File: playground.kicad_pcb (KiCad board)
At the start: 2 copper layers, 80 x 50 mm, 56 parts, among them IC1 TXU0101DBVR, IC11 LM3940IMP-3.3_NOPB, IC2 TXU0101DBVR, IC3 TXU0101DBVR, IC4 TXU0101DBVR, IC5 TXU0101DBVR, IC6 TXU0101DBVR, IC7 TXU0101DBVR, IC8 TXU0101DBVR, IC9 L293DD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

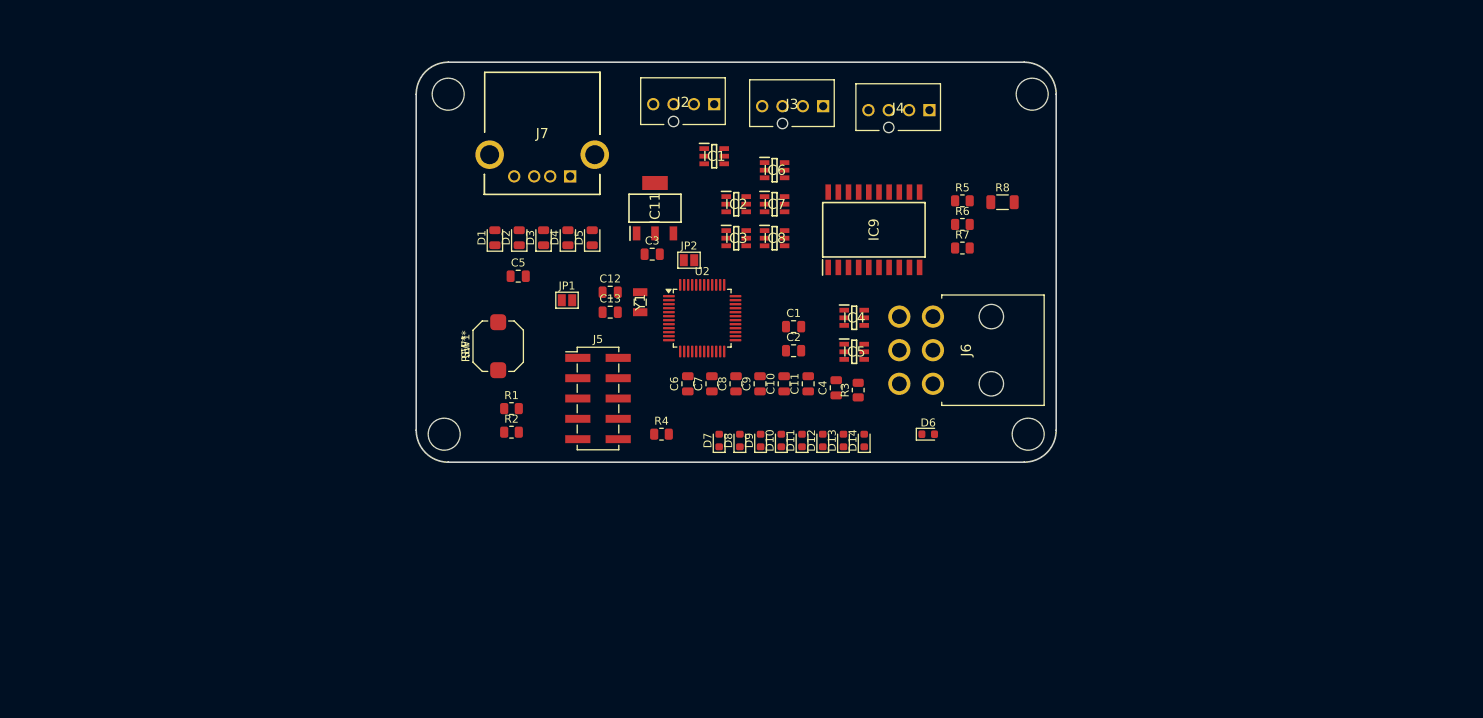
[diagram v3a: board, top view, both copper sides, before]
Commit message: Added LEDs and testpoints
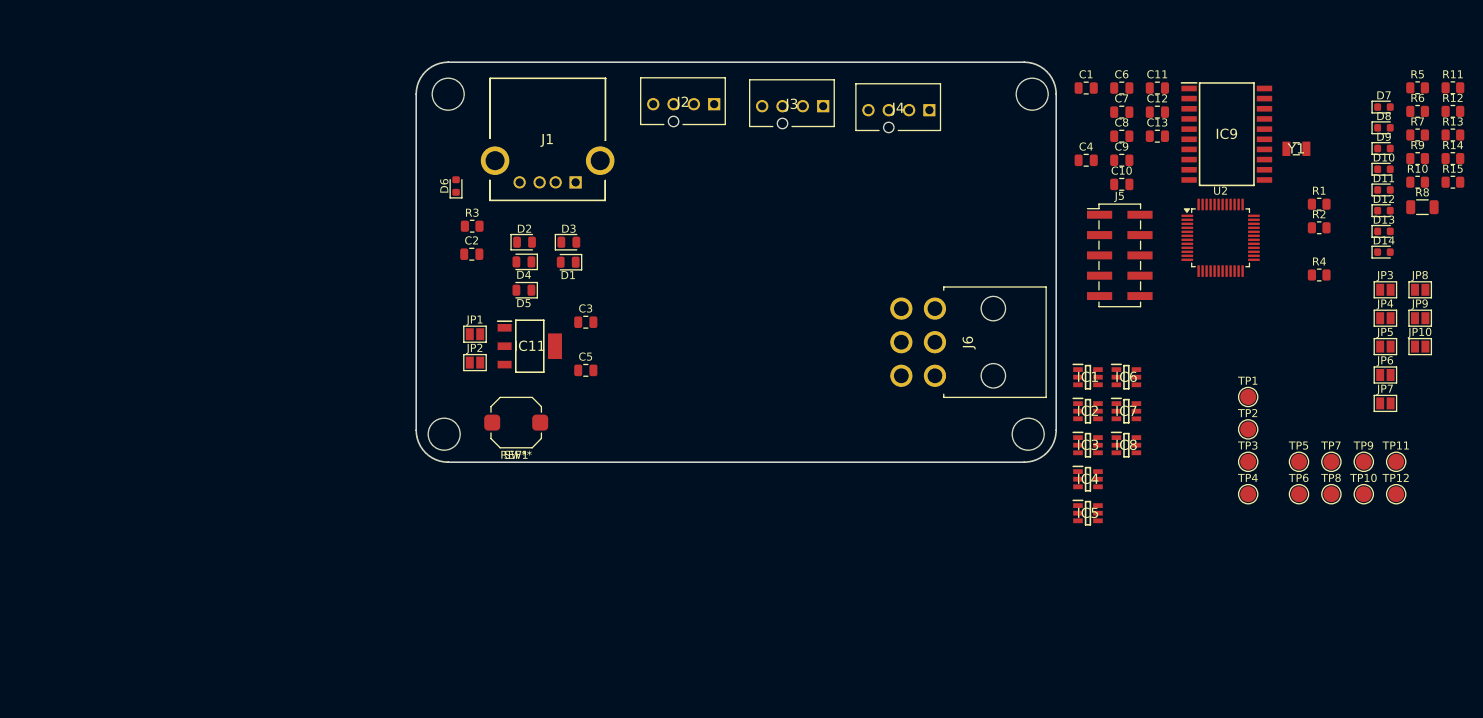
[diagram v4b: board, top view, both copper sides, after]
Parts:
- removed J7: USB_A, custom_footprints:676432910
- added J1: 67643-2910, custom_footprints:676432910, F.Cu at (119.9, 65.0)
- added JP10: SolderJumper_2_Open, Jumper:SolderJumper-2_P1.3mm_Open_Pad1.0x1.5mm, F.Cu at (225.5, 85.5)
- added JP3: SolderJumper_2_Open, Jumper:SolderJumper-2_P1.3mm_Open_Pad1.0x1.5mm, F.Cu at (221.2, 78.5)
- added JP4: SolderJumper_2_Open, Jumper:SolderJumper-2_P1.3mm_Open_Pad1.0x1.5mm, F.Cu at (221.2, 82.0)
- added JP5: SolderJumper_2_Open, Jumper:SolderJumper-2_P1.3mm_Open_Pad1.0x1.5mm, F.Cu at (221.2, 85.5)
- added JP6: SolderJumper_2_Open, Jumper:SolderJumper-2_P1.3mm_Open_Pad1.0x1.5mm, F.Cu at (221.2, 89.1)
- added JP7: SolderJumper_2_Open, Jumper:SolderJumper-2_P1.3mm_Open_Pad1.0x1.5mm, F.Cu at (221.2, 92.7)
- added JP8: SolderJumper_2_Open, Jumper:SolderJumper-2_P1.3mm_Open_Pad1.0x1.5mm, F.Cu at (225.5, 78.5)
- added JP9: SolderJumper_2_Open, Jumper:SolderJumper-2_P1.3mm_Open_Pad1.0x1.5mm, F.Cu at (225.5, 82.0)
- added R10: 51R, Resistor_SMD:R_0805_2012Metric, F.Cu at (225.2, 65.0)
- added R11: 20R, Resistor_SMD:R_0805_2012Metric, F.Cu at (229.6, 53.2)
- added R12: 20R, Resistor_SMD:R_0805_2012Metric, F.Cu at (229.6, 56.1)
- added R13: 20R, Resistor_SMD:R_0805_2012Metric, F.Cu at (229.6, 59.1)
- added R14: 20R, Resistor_SMD:R_0805_2012Metric, F.Cu at (229.6, 62.0)
- added R15: 20R, Resistor_SMD:R_0805_2012Metric, F.Cu at (229.6, 65.0)
- added R9: 51R, Resistor_SMD:R_0805_2012Metric, F.Cu at (225.2, 62.0)
- added TP1: TestPoint, TestPoint:TestPoint_Pad_D2.0mm, F.Cu at (204.0, 91.8)
- added TP10: TestPoint, TestPoint:TestPoint_Pad_D2.0mm, F.Cu at (218.4, 104.0)
- added TP11: TestPoint, TestPoint:TestPoint_Pad_D2.0mm, F.Cu at (222.5, 100.0)
- added TP12: TestPoint, TestPoint:TestPoint_Pad_D2.0mm, F.Cu at (222.5, 104.0)
- added TP2: TestPoint, TestPoint:TestPoint_Pad_D2.0mm, F.Cu at (204.0, 95.9)
- added TP3: TestPoint, TestPoint:TestPoint_Pad_D2.0mm, F.Cu at (204.0, 100.0)
- added TP4: TestPoint, TestPoint:TestPoint_Pad_D2.0mm, F.Cu at (204.0, 104.0)
- added TP5: TestPoint, TestPoint:TestPoint_Pad_D2.0mm, F.Cu at (210.3, 100.0)
- added TP6: TestPoint, TestPoint:TestPoint_Pad_D2.0mm, F.Cu at (210.3, 104.0)
- added TP7: TestPoint, TestPoint:TestPoint_Pad_D2.0mm, F.Cu at (214.4, 100.0)
- added TP8: TestPoint, TestPoint:TestPoint_Pad_D2.0mm, F.Cu at (214.4, 104.0)
- added TP9: TestPoint, TestPoint:TestPoint_Pad_D2.0mm, F.Cu at (218.4, 100.0)
- D14: value GENERAL_BOARD_1_IND -> GENERAL_BOARD_2_IND
- moved R1 104.1 mm to (212.9, 67.8)
- moved R2 104.1 mm to (212.9, 70.7)
- moved D7 93.0 mm to (221.0, 55.6), turned to 0 degrees
- moved D8 89.5 mm to (221.0, 58.2), turned to 0 degrees
- moved D9 86.0 mm to (221.0, 60.8), turned to 0 degrees
- moved R4 84.6 mm to (212.9, 76.6)
- moved Y1 84.2 mm to (210.0, 60.8), turned to 0 degrees
- moved D10 82.6 mm to (221.0, 63.4), turned to 0 degrees
- moved D11 79.2 mm to (221.0, 66.0), turned to 0 degrees
- moved D12 75.8 mm to (221.0, 68.6), turned to 0 degrees
- moved D13 72.4 mm to (221.0, 71.2), turned to 0 degrees
- moved C12 72.0 mm to (192.6, 56.2)
- moved C13 71.8 mm to (192.6, 59.2)
- moved D14 69.1 mm to (221.0, 73.7), turned to 0 degrees
- moved J5 67.6 mm to (187.9, 74.2)
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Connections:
- D1 pad 2: /USB_D+ -> /USB_D-
- D10 pad 2: /FAN_PWM_IND_LED -> /LEDs/FAN_PWM_IND_LED_5v
- D11 pad 2: /VALVE_OPEN_IND_LED -> /LEDs/VALVE_OPEN_IND_LED_5v
- D12 pad 2: /VALVE_CLOSED_IND_LED -> /LEDs/VALVE_CLOSED_IND_LED_5v
- D13 pad 2: /GENERAL_BOARD_1_IND_LED -> /LEDs/GENERAL_BOARD_1_IND_LED_3v3
- D14 pad 2: /GENERAL_BOARD_1_IND_LED -> /LEDs/GENERAL_BOARD_2_IND_LED_3v3
- D2 pad 2: /USB_D- -> /USB_D+
- D3 pad 1: /USB_D+ -> /USB_D-
- D4 pad 1: /USB_D- -> /USB_D+
- D6 pad 2: /5v_USB_PWR_IND_LED -> /LEDs/5v_USB_PWR_IND_LED
- D7 pad 2: +3V3 -> /LEDs/3v3_PWR_IND_LED
- D8 pad 2: +12V -> /LEDs/12v_PWR_IND_LED
- D9 pad 2: /PUMP_PWM_IND_LED -> /LEDs/PUMP_PWM_IND_LED_5v
- J2 pad 3: /PumpSense_5v -> Net-(JP4-B)
- J2 pad 4: /PumpCtrl_5v -> Net-(JP3-B)
- J3 pad 3: /FanSense_5v -> Net-(JP6-B)
- J3 pad 4: /FanCtrl_5v -> Net-(JP5-B)
- J4 pad 1: /ValveSense2_5v -> Net-(JP10-B)
- J4 pad 2: /ValveSense1_5v -> Net-(JP9-B)
- J4 pad 3: /ValveOutput1_12v -> Net-(JP8-B)
- J4 pad 4: /ValveOutput2_12v -> Net-(JP7-B)
- R5 pad 1: GND -> /LEDs/3v3_PWR_IND_LED
- R8 pad 2: unconnected-(R8-Pad2) -> /LEDs/12v_PWR_IND_LED

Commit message: removed jumpers
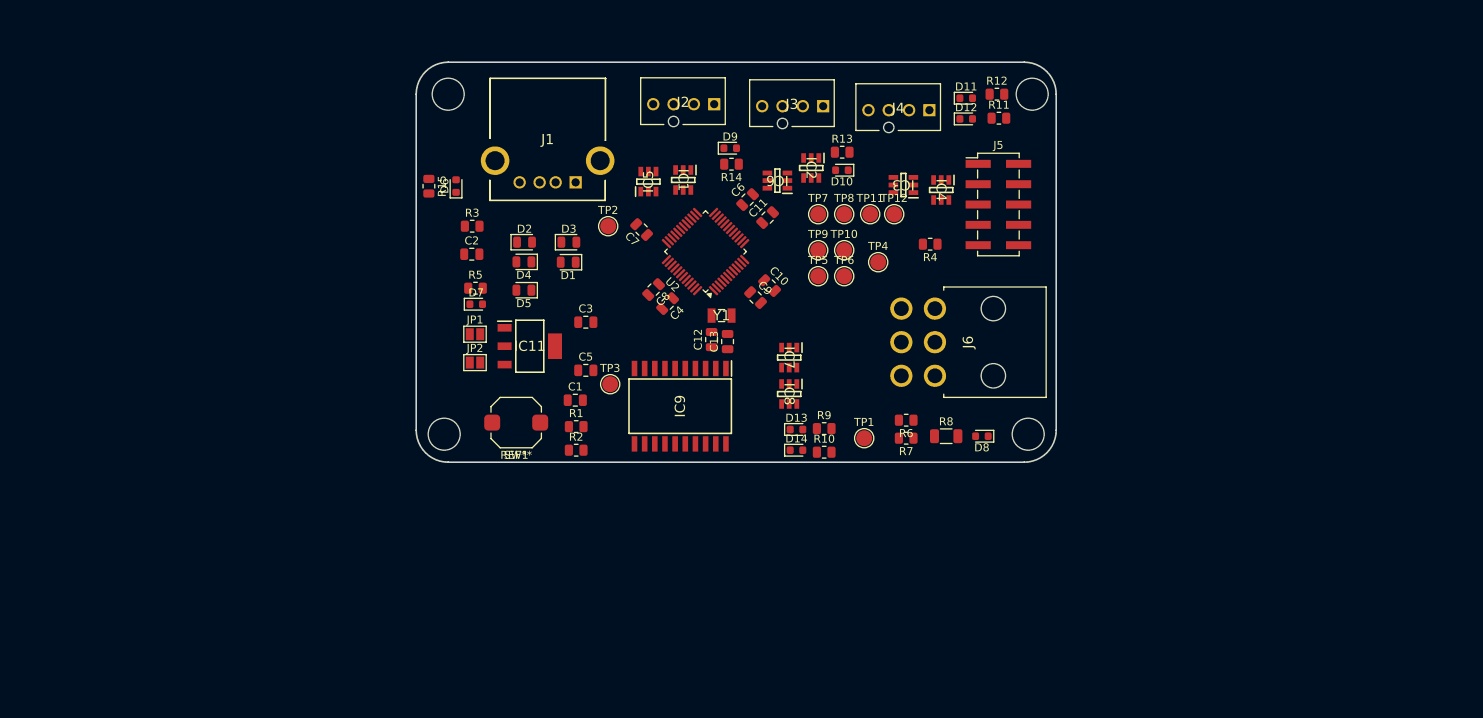
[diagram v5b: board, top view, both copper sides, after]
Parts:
- removed JP10, JP3, JP4, JP5, JP6, JP7, JP8, JP9: SolderJumper_2_Open, Jumper:SolderJumper-2_P1.3mm_Open_Pad1.0x1.5mm
- moved R15 128.0 mm to (101.6, 65.5), turned to -90 degrees
- moved R5 120.4 mm to (107.4, 78.2)
- moved D7 116.1 mm to (107.5, 80.2)
- moved R1 96.9 mm to (120.0, 95.5)
- moved R2 96.9 mm to (120.0, 98.5)
- moved R14 90.2 mm to (139.4, 62.8), turned to 180 degrees
- moved TP2 83.9 mm to (124.0, 70.5)
- moved D9 81.7 mm to (139.2, 60.8)
- moved R10 81.5 mm to (151.0, 98.8)
- moved R9 81.5 mm to (151.0, 95.8)
- moved TP3 80.3 mm to (124.2, 90.2)
- moved D14 77.5 mm to (147.5, 98.5)
- moved D13 77.5 mm to (147.5, 95.9)
- moved R13 76.4 mm to (153.2, 61.2)
- moved IC9 76.3 mm to (133.0, 93.0), turned to -90 degrees
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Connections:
- J2 pad 3: Net-(JP4-B) -> /PumpSense_5v
- J2 pad 4: Net-(JP3-B) -> /PumpCtrl_5v
- J3 pad 3: Net-(JP6-B) -> /FanSense_5v
- J3 pad 4: Net-(JP5-B) -> /FanCtrl_5v
- J4 pad 1: Net-(JP10-B) -> /ValveSense2_5v
- J4 pad 2: Net-(JP9-B) -> /ValveSense1_5v
- J4 pad 3: Net-(JP8-B) -> /ValveOutput1_12v
- J4 pad 4: Net-(JP7-B) -> /ValveOutput2_12v

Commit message: Changed board size to 80x80mm
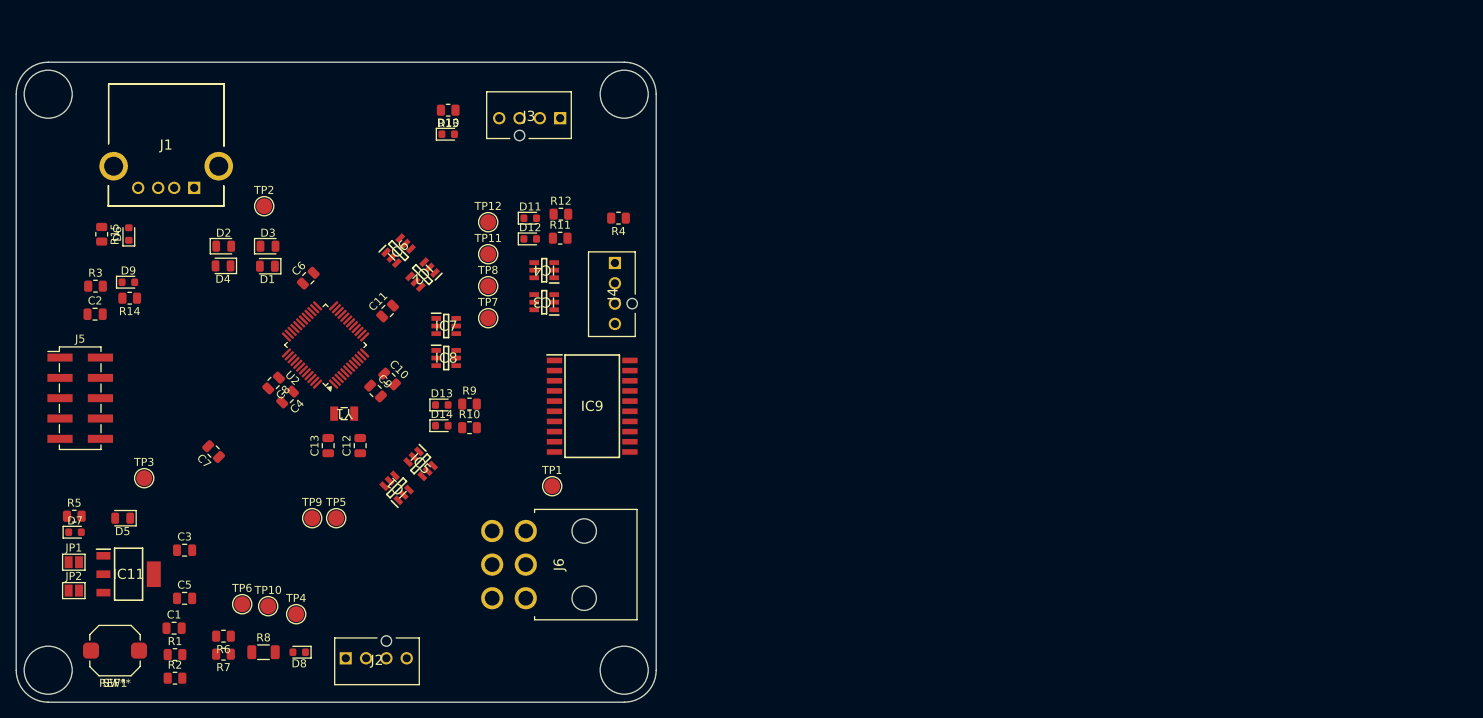
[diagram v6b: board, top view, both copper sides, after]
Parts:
- moved J5 117.3 mm to (58.0, 92.0)
- moved D8 89.5 mm to (85.4, 123.8)
- moved R6 89.5 mm to (75.9, 121.8)
- moved R7 89.5 mm to (75.9, 124.0)
- moved R8 89.5 mm to (80.9, 123.8)
- moved TP6 85.7 mm to (78.2, 117.8)
- moved TP4 85.0 mm to (85.0, 119.0)
- moved TP10 84.6 mm to (81.5, 118.0)
- moved J2 83.2 mm to (91.2, 124.5), turned to 180 degrees
- moved D9 77.1 mm to (64.0, 77.5)
- moved R14 77.1 mm to (64.2, 79.5)
- moved TP9 71.6 mm to (87.0, 107.0)
- moved TP5 67.4 mm to (90.0, 107.0)
- moved C7 60.3 mm to (74.7, 98.7)
- moved TP3 59.4 mm to (66.0, 102.0)
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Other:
- board size 80 x 50 mm -> 80 x 80 mm

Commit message: Updated layout and schem
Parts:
- removed C9: 1u, Capacitor_SMD:C_0805_2012Metric
- TP1, TP10, TP11, TP12, TP2, TP3, TP4, TP5, TP6, TP7, TP8, TP9: footprint TestPoint:TestPoint_Pad_D2.0mm -> TestPoint:TestPoint_Pad_D1.0mm
- moved R4 63.2 mm to (67.0, 94.0), turned to -135 degrees
- moved IC11 58.0 mm to (91.0, 62.6)
- moved JP1 57.5 mm to (82.0, 60.6), turned to 90 degrees
- moved C5 54.2 mm to (85.0, 64.6), turned to 90 degrees
- moved JP2 54.1 mm to (85.0, 69.6), turned to -90 degrees
- moved C3 52.2 mm to (85.0, 60.6), turned to -90 degrees
- moved TP10 50.4 mm to (106.0, 74.0)
- moved TP6 49.5 mm to (101.5, 74.0)
- moved R5 48.8 mm to (89.0, 69.6)
- moved D7 48.5 mm to (89.0, 72.0)
- moved TP2 48.4 mm to (74.5, 116.0)
- moved R8 42.4 mm to (116.0, 99.9)
- moved D8 42.4 mm to (120.4, 99.9)
- moved R6 42.2 mm to (112.0, 99.9), turned to -90 degrees
- moved R7 41.7 mm to (110.0, 99.9), turned to -90 degrees
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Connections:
- net Net-(R6-Pad1) renamed /LEDs/12v_PWD_LED_VOL_DIV
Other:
- board text added: "1"
- board text added: "12V"
- board text added: "2"
- board text added: "3V3"
- board text added: "5V"
- board text added: "Ctrl"
- board text added: "Fan"
- board text added: "GND"
- board text added: "Power Test Points"
- board text added: "Sense"
- board text added: "Valve"

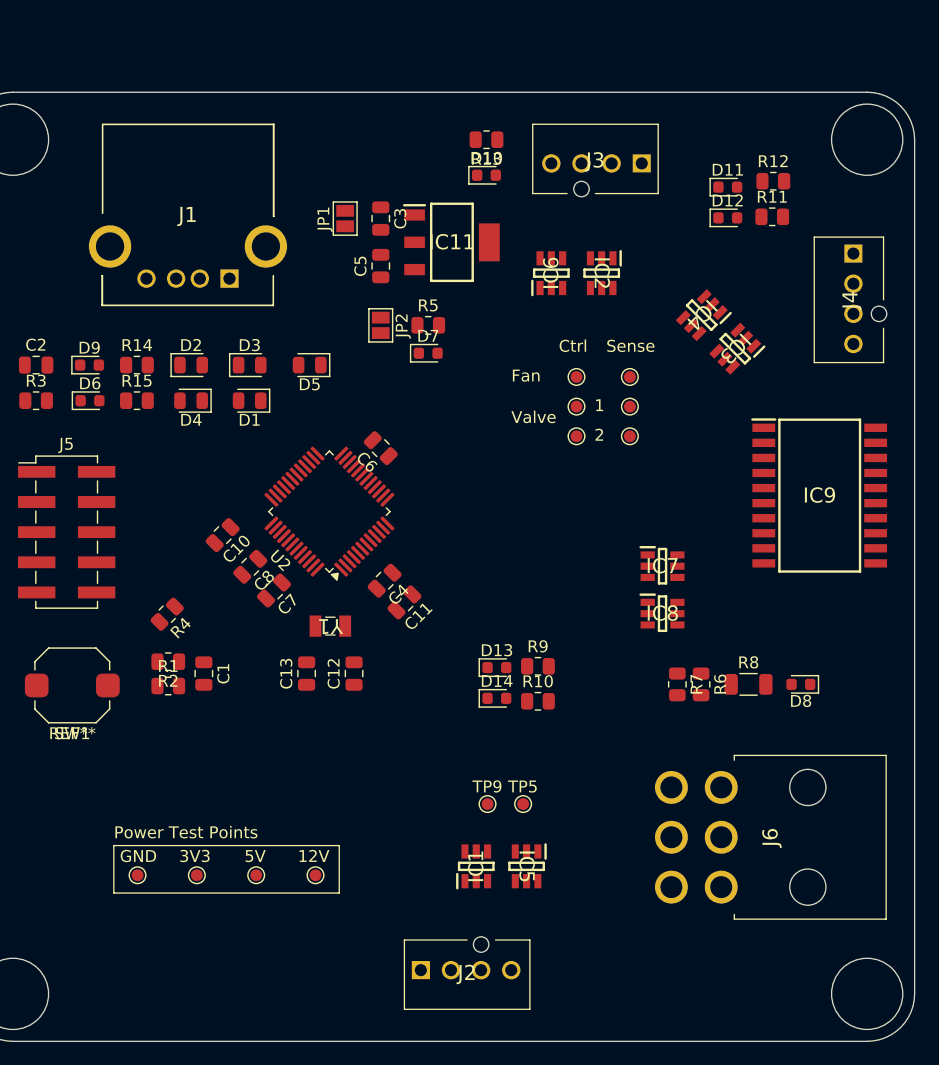
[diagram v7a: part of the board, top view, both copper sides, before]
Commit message: Layout of indicator LEDs. Shrank design space
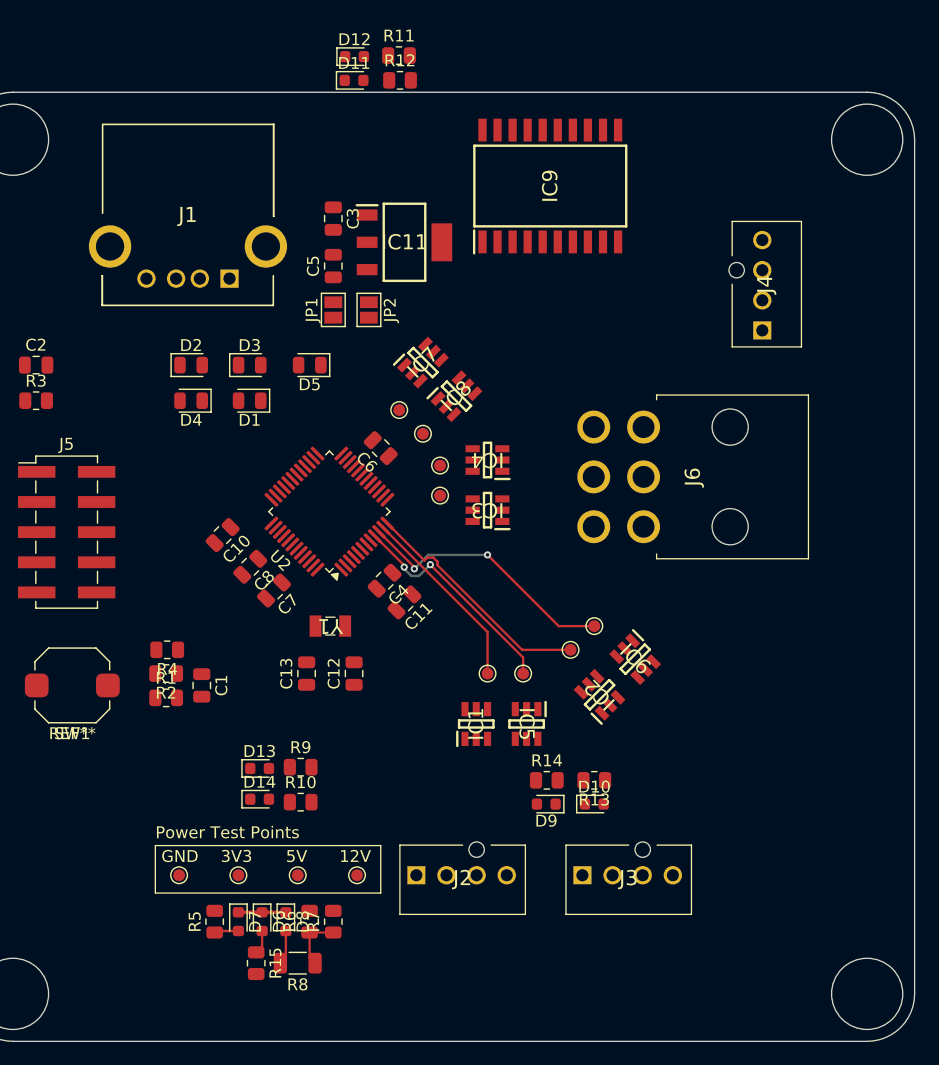
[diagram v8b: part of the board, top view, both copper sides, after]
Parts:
- moved J3 60.2 mm to (102.0, 116.0), turned to 180 degrees
- moved R13 54.8 mm to (103.0, 108.0)
- moved D10 53.8 mm to (103.0, 110.0)
- moved D9 53.4 mm to (99.0, 110.0), turned to 180 degrees
- moved R5 53.4 mm to (71.0, 119.9), turned to 90 degrees
- moved D7 50.5 mm to (73.0, 119.9), turned to -90 degrees
- moved R14 49.2 mm to (99.0, 108.0)
- moved R15 48.5 mm to (74.5, 123.4), turned to -90 degrees
- moved D8 47.8 mm to (77.0, 119.9), turned to -90 degrees
- moved D6 46.2 mm to (75.0, 119.9), turned to -90 degrees
- moved R8 44.7 mm to (78.0, 123.4), turned to 180 degrees
- moved R6 38.6 mm to (79.0, 119.9), turned to 90 degrees
- moved IC2 35.5 mm to (103.4, 100.8), turned to 135 degrees
- moved R7 35.2 mm to (81.0, 119.9), turned to 90 degrees
- moved IC9 34.6 mm to (99.3, 57.9), turned to 90 degrees
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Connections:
- D10 pad 2: /LEDs/FAN_PWM_IND_LED_5v -> /FanCtrl_5v
- D11 pad 2: /LEDs/VALVE_OPEN_IND_LED_5v -> /ValveSense2_5v
- D12 pad 2: /LEDs/VALVE_CLOSED_IND_LED_5v -> /ValveSense1_5v
- D9 pad 2: /LEDs/PUMP_PWM_IND_LED_5v -> /PumpCtrl_5v
- IC9 pad 3: /ValveOutput1_12v -> /ValveOutput2_12v
- IC9 pad 8: /ValveOutput2_12v -> /ValveOutput1_12v
- R11 pad 1: /LEDs/VALVE_CLOSED_IND_LED_5v -> /ValveSense1_5v
- R12 pad 1: /LEDs/VALVE_OPEN_IND_LED_5v -> /ValveSense2_5v
- R13 pad 1: /LEDs/FAN_PWM_IND_LED_5v -> /FanCtrl_5v
- R14 pad 1: /LEDs/PUMP_PWM_IND_LED_5v -> /PumpCtrl_5v
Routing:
- net /FanCtrl_3v3: track 0.00 -> 22.5 mm, vias 0 -> 2
- net /FanSense_3v3: track 0.00 -> 20.2 mm
- net /PumpCtrl_3v3: track 0.00 -> 19.0 mm, vias 0 -> 2
- net /PumpSense_3v3: track 0.00 -> 15.9 mm
- net /LEDs/12v_PWD_LED_VOL_DIV: track 0.00 -> 4.78 mm
- net GND: track 0.00 -> 4.00 mm
- net /LEDs/12v_PWR_IND_LED: track 0.00 -> 2.90 mm
- net /LEDs/3v3_PWR_IND_LED: track 0.00 -> 2.05 mm
- net /LEDs/5v_USB_PWR_IND_LED: track 0.00 -> 2.01 mm
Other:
- board text removed: "1"
- board text removed: "2"
- board text removed: "Ctrl"
- board text removed: "Fan"
- board text removed: "Sense"
- board text removed: "Valve"
